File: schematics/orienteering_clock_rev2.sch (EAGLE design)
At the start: 54 parts, among them IC1 TPIC6B595N, IC2 TPIC6B595N, J2 ICSP, Q1 IRFU9024V, Q2 IRFU9024V, Q3 IRFU9024V, Q4 IRFU9024V, Q5 IRFU9024V, Q6 IRFU9024V, T1 BC547, Y1 16MHz

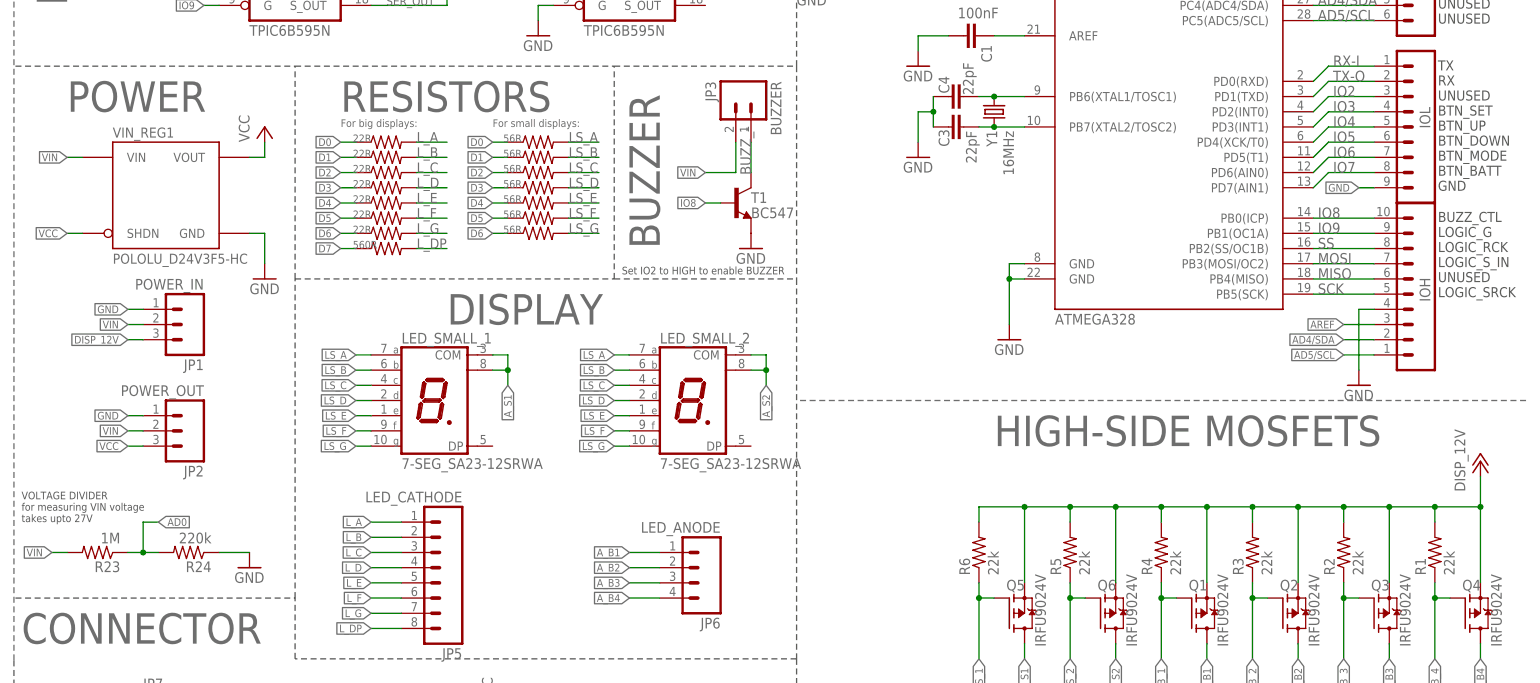
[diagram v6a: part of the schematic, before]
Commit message: schematics: modified POWER packages/schema, texts on top silkscreen
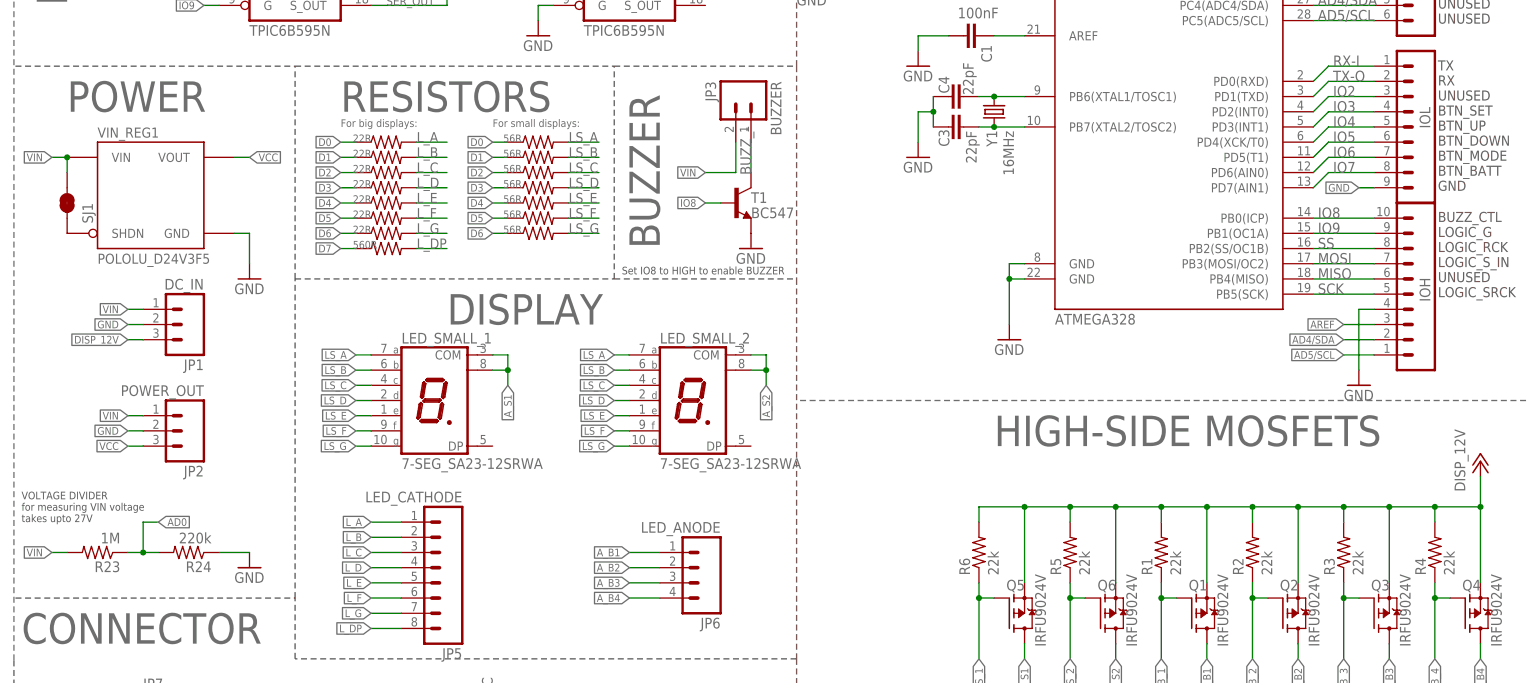
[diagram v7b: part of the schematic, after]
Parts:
- added SJ1: SHDN_PULLUP, SparkFun-Passives:JUMPER-PAD-2-NC_BY_TRACE
- JP1: value POWER_IN -> DC_IN; device SparkFun-Connectors:M03POLAR -> SparkFun-Connectors:M03JST-PTH
- JP2: device SparkFun-Connectors:M03POLAR -> SparkFun-Connectors:M03LOCK
- JP3: device SparkFun-Connectors:M02POLAR -> SparkFun-Connectors:M02LOCK
- VIN_REG1: value POLOLU_D24V3F5-HC -> POLOLU_D24V3F5
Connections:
- new net N$1: SJ1.2, VIN_REG1.SHDN
- net B_1: now also R1.1; no longer R4.1
- net B_2: now also R2.1; no longer R3.1
- net B_3: now also R3.1; no longer R2.1
- net B_4: now also R4.1; no longer R1.1
- net GND: now also JP1.2, JP2.2; no longer JP1.1, JP2.1
- net VCC: no longer VIN_REG1.SHDN
- net VIN: now also JP1.1, JP2.1, SJ1.1; no longer JP1.2, JP2.2
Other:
- note added: "Set IO8 to HIGH to enable BUZZER"
- note removed: "Set IO2 to HIGH to enable BUZZER"
- moved on the sheet: R1, R2, R3, R4, VIN_REG1

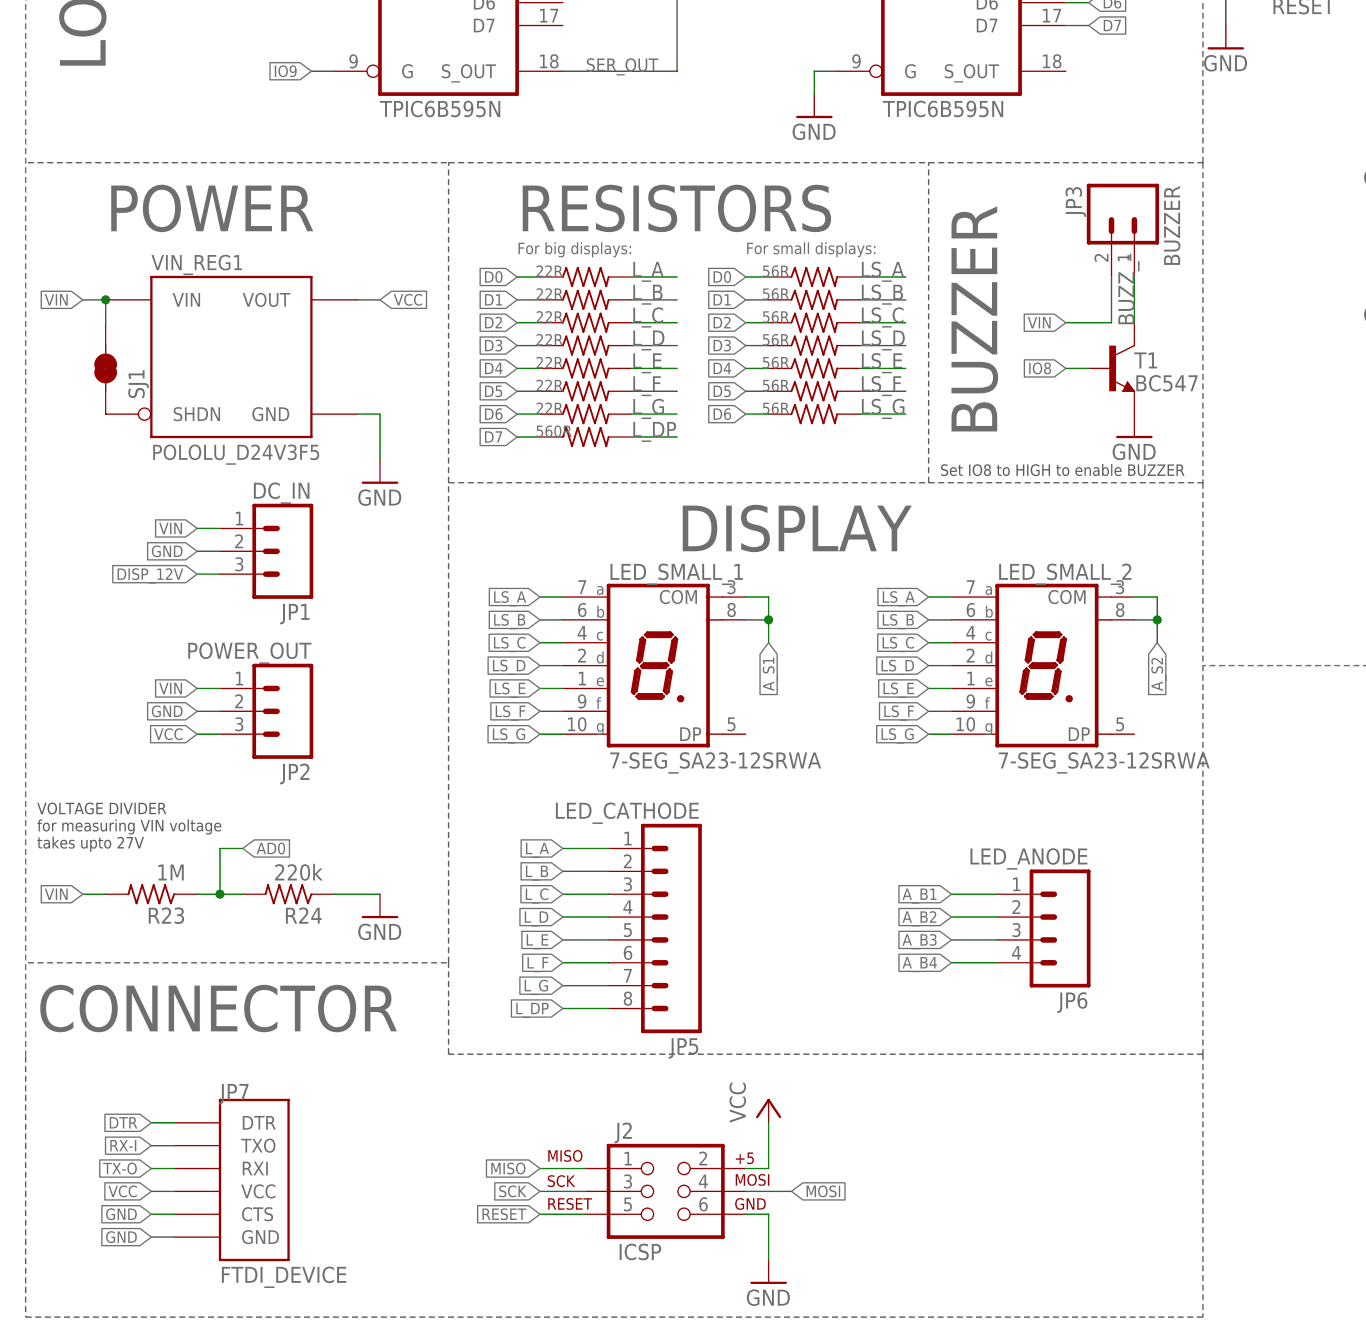
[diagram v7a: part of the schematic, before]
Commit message: schematics: added option to use LM7805 as voltage regulator
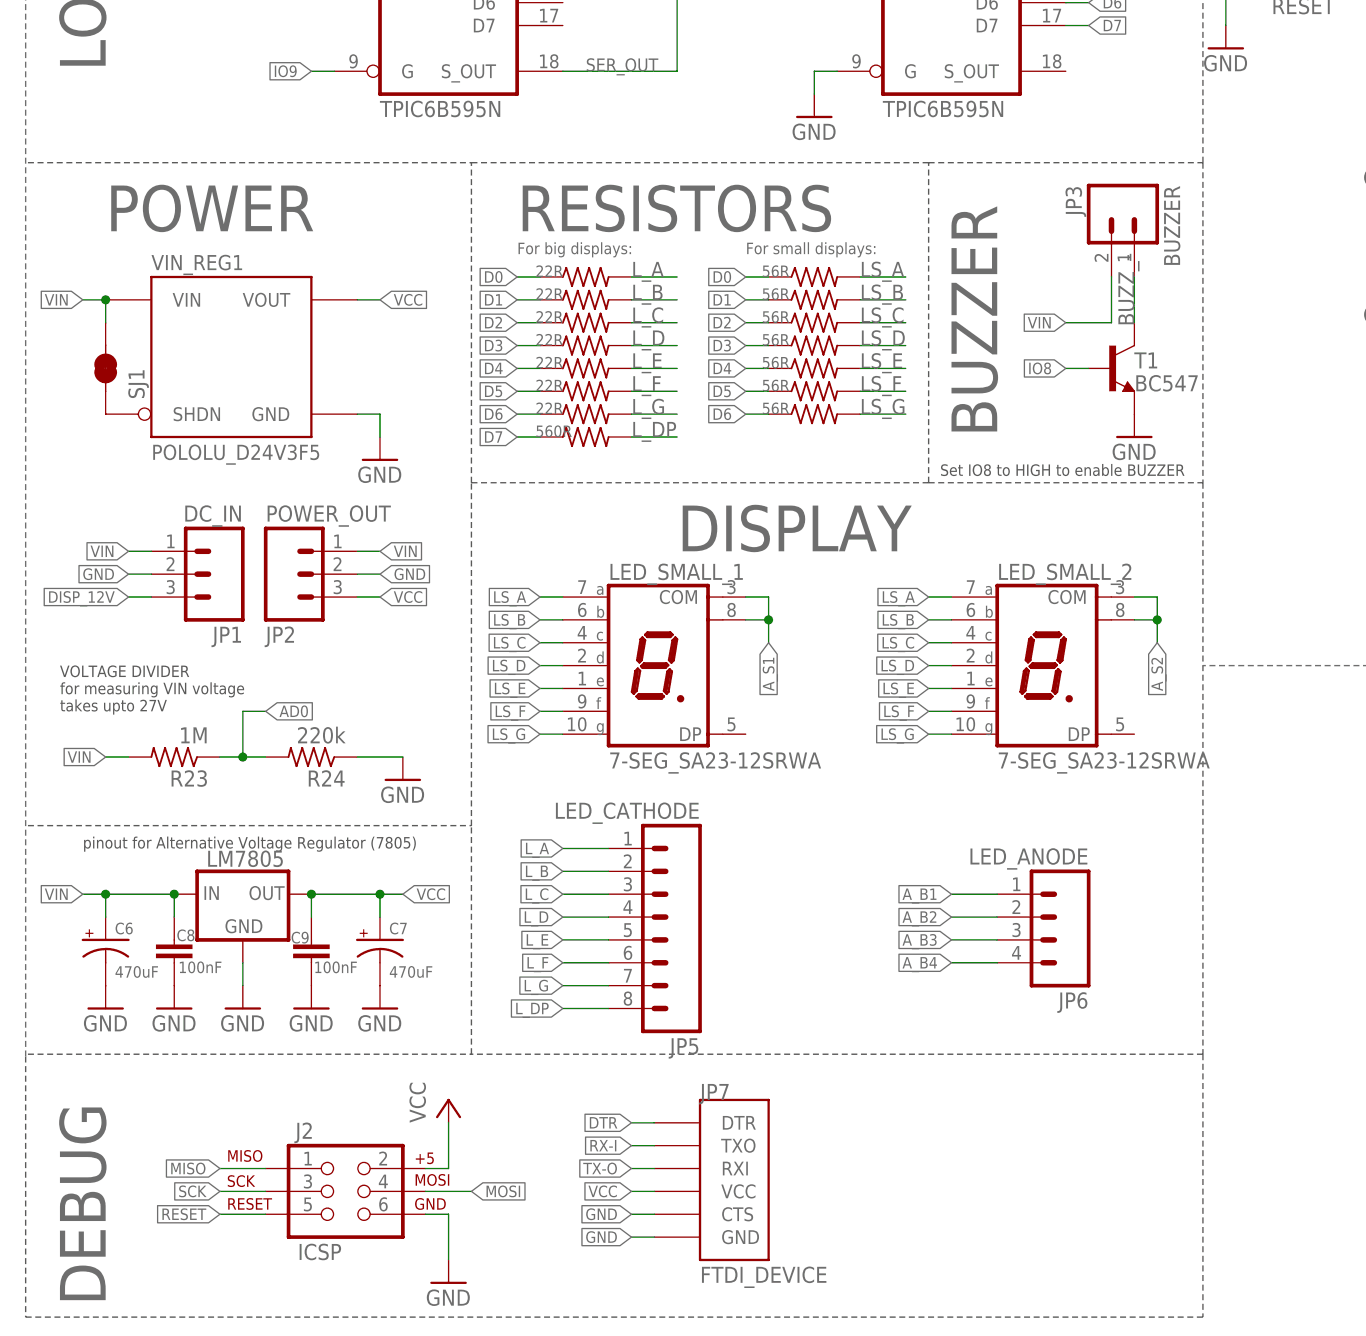
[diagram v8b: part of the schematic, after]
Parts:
- added C6, C7: 470uF, SparkFun-Passives:CAP_POLPTH1
- added C8, C9: 100nF, SparkFun-Passives:CAPPTH
- added LM7805: (no value), v-reg:78XXS
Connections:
- net GND: now also C6.-, C7.-, C8.2, C9.2, LM7805.GND
- net VCC: now also C7.+, C9.1, LM7805.OUT
- net VIN: now also C6.+, C8.1, LM7805.IN
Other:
- note added: "DEBUG"
- note added: "pinout for Alternative Voltage Regulator (7805)"
- note removed: "CONNECTOR"
- moved on the sheet: J2, JP1, JP2, JP7, R23, R24
